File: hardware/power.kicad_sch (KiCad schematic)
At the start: 31 parts, among them J2 batt, Q1 AO3400A, SW57 MK-12C02-G020, U3 BQ24075RGT, U4 TLV62569DBV

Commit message: Add MY-18650-01 footprint and 3d model
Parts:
- removed J2: batt, Battery:BatteryHolder_Keystone_1042_1x18650, symbol Connector_Generic:Conn_01x02
- added J2, J5: MY-18650-01, lib:MY-18650-01, symbol Connector:Conn_01x01_Socket
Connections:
- net GND: now also J2.1 (Pin_1)
- net at C3.1, U3.2 (BAT), U3.3 (BAT): now also J5.1 (Pin_1)
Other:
- note added: "Battery terminals"
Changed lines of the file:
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@@
 		)
 	)
+	(rectangle
+		(start 156.21 132.08)
+		(end 165.1 139.7)
+		(stroke
+			(width 0)
+			(type dash)
+		)
+		(fill
+			(type none)
+		)
+	)
 	(image
 		(at 222.25 39.37)
@@
 		)
 	)
+	(text "Battery\nterminals"
+		(exclude_from_sim no)
+		(at 160.782 142.24 0)
+		(effects
+			(font
+				(size 1.27 1.27)
+			)
+		)
+	)
 	(text "100mA"
 		(exclude_from_sim no)
@@
 	)
 	(symbol
+		(lib_id "Connector:Conn_01x01_Socket")
+		(at 161.29 137.16 0)
+		(unit 1)
+		(exclude_from_sim no)
+		(in_bom yes)
+		(on_board yes)
+		(dnp no)
+		(property "Reference" "J2"
+			(at 162.306 137.16 0)
+			(effects
+				(font
+					(size 1.27 1.27)
+				)
+				(justify left)
+			)
+		)
+		(property "Value" "MY-18650-01"
+			(at 162.56 138.4299 0)
+			(effects
+				(font
+					(size 1.27 1.27)
+				)
+				(justify left)
+				(hide yes)
+			)
+		)
+		(property "Footprint" "lib:MY-18650-01"
+			(at 161.29 137.16 0)
+			(effects
+				(font
+					(size 1.27 1.27)
+				)
+				(hide yes)
+			)
+		)
+		(property "Datasheet" "~"
+			(at 161.29 137.16 0)
+			(effects
+				(font
+					(size 1.27 1.27)
+				)
+				(hide yes)
+			)
+		)
+		(property "Description" "Generic connector, single row, 01x01, script generated"
+			(at 161.29 137.16 0)
+			(effects
+				(font
+					(size 1.27 1.27)
+				)
+				(hide yes)
+			)
+		)
+		(property "LCSC" "C2979183"
+			(at 161.29 137.16 0)
+			(effects
+				(font
+					(size 1.27 1.27)
+				)
+				(hide yes)
+			)
+		)
+		(pin "1"
+		)
+		(instances
+			(project "badge"
+				(path "/dc4a3d77-b0f8-4e90-a4be-3e93c7025348/fa1edb42-107e-4301-94d6-2222638475c5"
+					(reference "J2")
+					(unit 1)
+				)
+			)
+		)
+	)
+	(symbol
 		(lib_id "power:VDD")
 		(at 113.03 31.75 0)
@@
 	)
 	(symbol
-		(lib_id "Connector_Generic:Conn_01x02")
-		(at 161.29 137.16 0)
-		(mirror x)
-		(unit 1)
-		(exclude_from_sim no)
-		(in_bom yes)
-		(on_board yes)
-		(dnp no)
-		(property "Reference" "J2"
-			(at 161.544 132.08 0)
-			(effects
-				(font
-					(size 1.27 1.27)
-				)
-			)
-		)
-		(property "Value" "batt"
-			(at 161.29 139.954 0)
-			(effects
-				(font
-					(size 1.27 1.27)
-				)
-			)
-		)
-		(property "Footprint" "Battery:BatteryHolder_Keystone_1042_1x18650"
-			(at 161.29 137.16 0)
-			(effects
-				(font
-					(size 1.27 1.27)
-				)
-				(hide yes)
-			)
-		)
-		(property "Datasheet" "~"
-			(at 161.29 137.16 0)
-			(effects
-				(font
-					(size 1.27 1.27)
-				)
-				(hide yes)
-			)
-		)
-		(property "Description" "Generic connector, single row, 01x02, script generated (kicad-library-utils/schlib/autogen/connector/)"
-			(at 161.29 137.16 0)
-			(effects
-				(font
-					(size 1.27 1.27)
-				)
-				(hide yes)
-			)
-		)
-		(pin "2"
-		)
-		(pin "1"
-		)
-		(instances
-			(project "badge"
-				(path "/dc4a3d77-b0f8-4e90-a4be-3e93c7025348/fa1edb42-107e-4301-94d6-2222638475c5"
-					(reference "J2")
-					(unit 1)
-				)
-			)
-		)
-	)
-	(symbol
 		(lib_id "power:GND")
 		(at 113.03 58.42 0)
@@
 					(unit 1)
 				)
+			)
+		)
+	)
+	(symbol
+		(lib_id "Connector:Conn_01x01_Socket")
+		(at 161.29 134.62 0)
+		(unit 1)
+		(exclude_from_sim no)
+		(in_bom yes)
+		(on_board yes)
+		(dnp no)
+		(property "Reference" "J5"
+			(at 162.306 134.62 0)
+			(effects
+				(font
+					(size 1.27 1.27)
+				)
+				(justify left)
+			)
+		)
+		(property "Value" "MY-18650-01"
+			(at 162.56 135.8899 0)
+			(effects
+				(font
+					(size 1.27 1.27)
+				)
+				(justify left)
+				(hide yes)
+			)
+		)
+		(property "Footprint" "lib:MY-18650-01"
+			(at 161.29 134.62 0)
+			(effects
+				(font
+					(size 1.27 1.27)
+				)
+				(hide yes)
+			)
+		)
+		(property "Datasheet" "~"
+			(at 161.29 134.62 0)
+			(effects
+				(font
+					(size 1.27 1.27)
+				)
+				(hide yes)
+			)
+		)
+		(property "Description" "Generic connector, single row, 01x01, script generated"
+			(at 161.29 134.62 0)
+			(effects
+				(font
+					(size 1.27 1.27)
+				)
+				(hide yes)
+			)
+		)
+		(property "LCSC" "C2979183"
+			(at 161.29 134.62 0)
+			(effects
+				(font
+					(size 1.27 1.27)
+				)
+				(hide yes)
+			)
+		)
+		(pin "1"
+		)
+		(instances
+			(project "badge"
+				(path "/dc4a3d77-b0f8-4e90-a4be-3e93c7025348/fa1edb42-107e-4301-94d6-2222638475c5"
+					(reference "J5")
+					(unit 1)
+				)

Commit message: Cleanup project library
Add hexpansion connector symbol, footprint and 3d
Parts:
- J2, J5: footprint lib:MY-18650-01 -> badge:MY-18650-01
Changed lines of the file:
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@@
 			)
 		)
-		(property "Footprint" "lib:MY-18650-01"
+		(property "Footprint" "badge:MY-18650-01"
 			(at 161.29 137.16 0)
 			(effects
@@
 			)
 		)
-		(property "Footprint" "lib:MY-18650-01"
+		(property "Footprint" "badge:MY-18650-01"
 			(at 161.29 134.62 0)
 			(effects

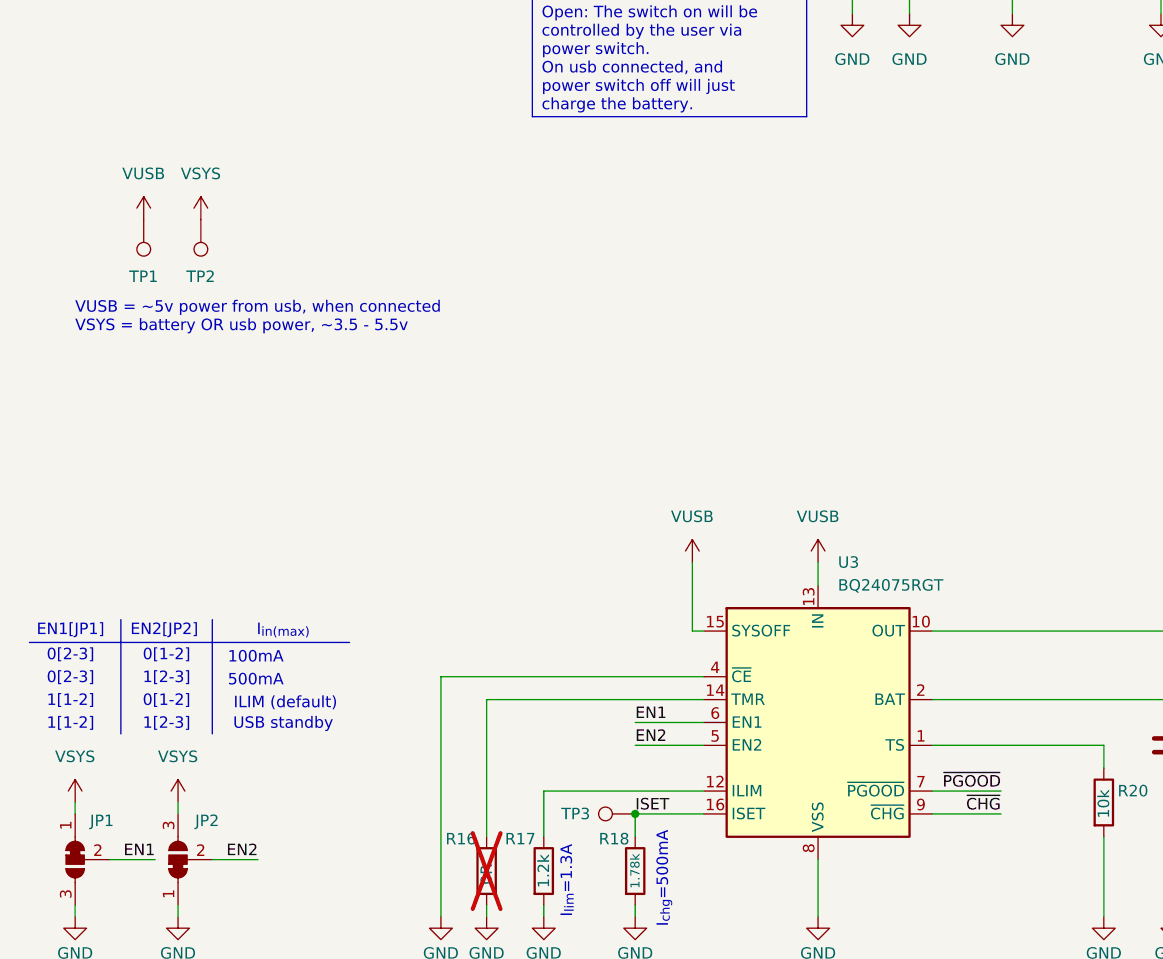
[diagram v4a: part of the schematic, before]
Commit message: Route all board
Fix CS missing for SD card
Add IMU symbol and footprint to the project lib
Finish esp32 pinswaps
Move non critical signals to the keyboard IO expander
Add power flag symbols
Fix Dpad pin type
Fix IMU pin type
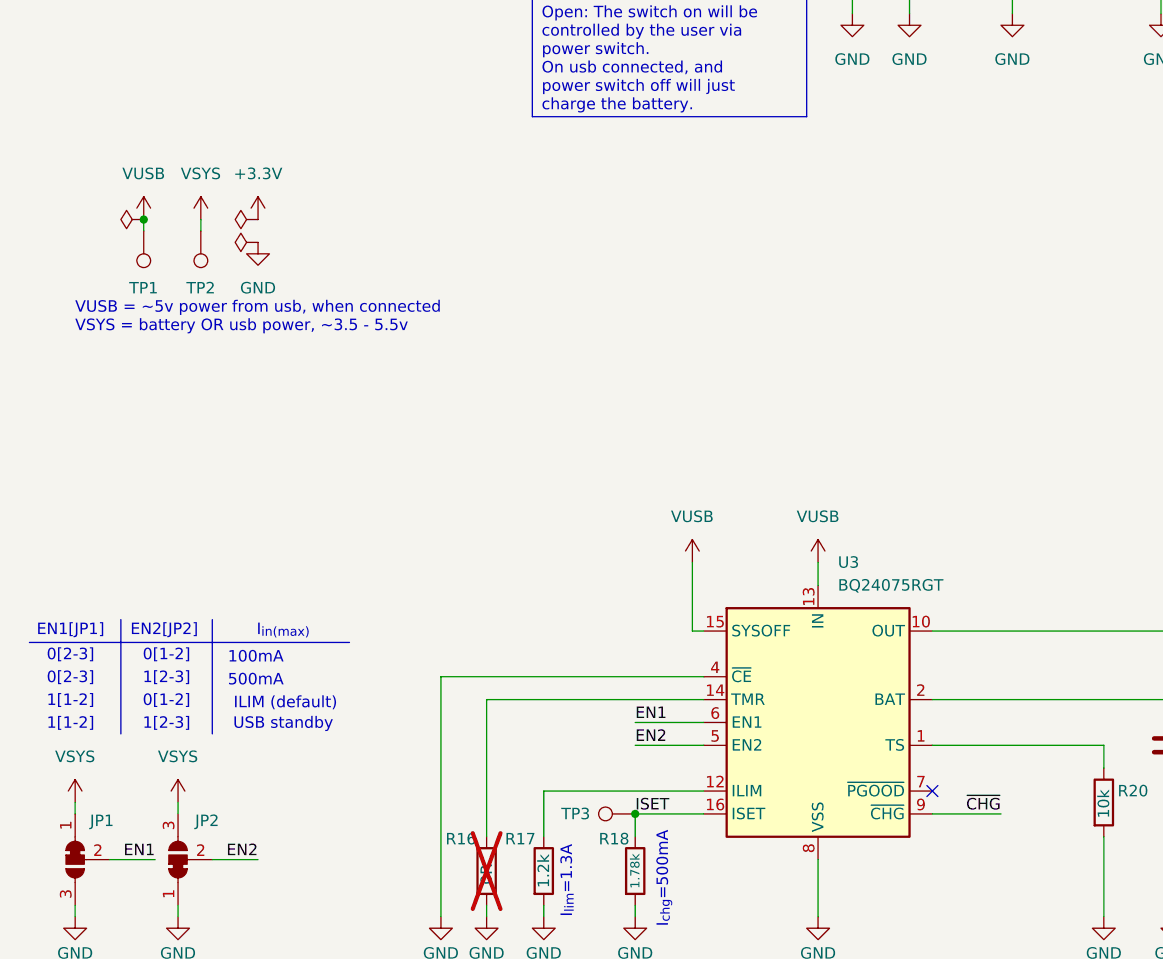
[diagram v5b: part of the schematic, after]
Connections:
- net ~{PGOOD}: no longer names the net of U3.7 (~{PGOOD})
- no-connect marks 0 -> 1
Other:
- moved on the sheet: TP1, TP2

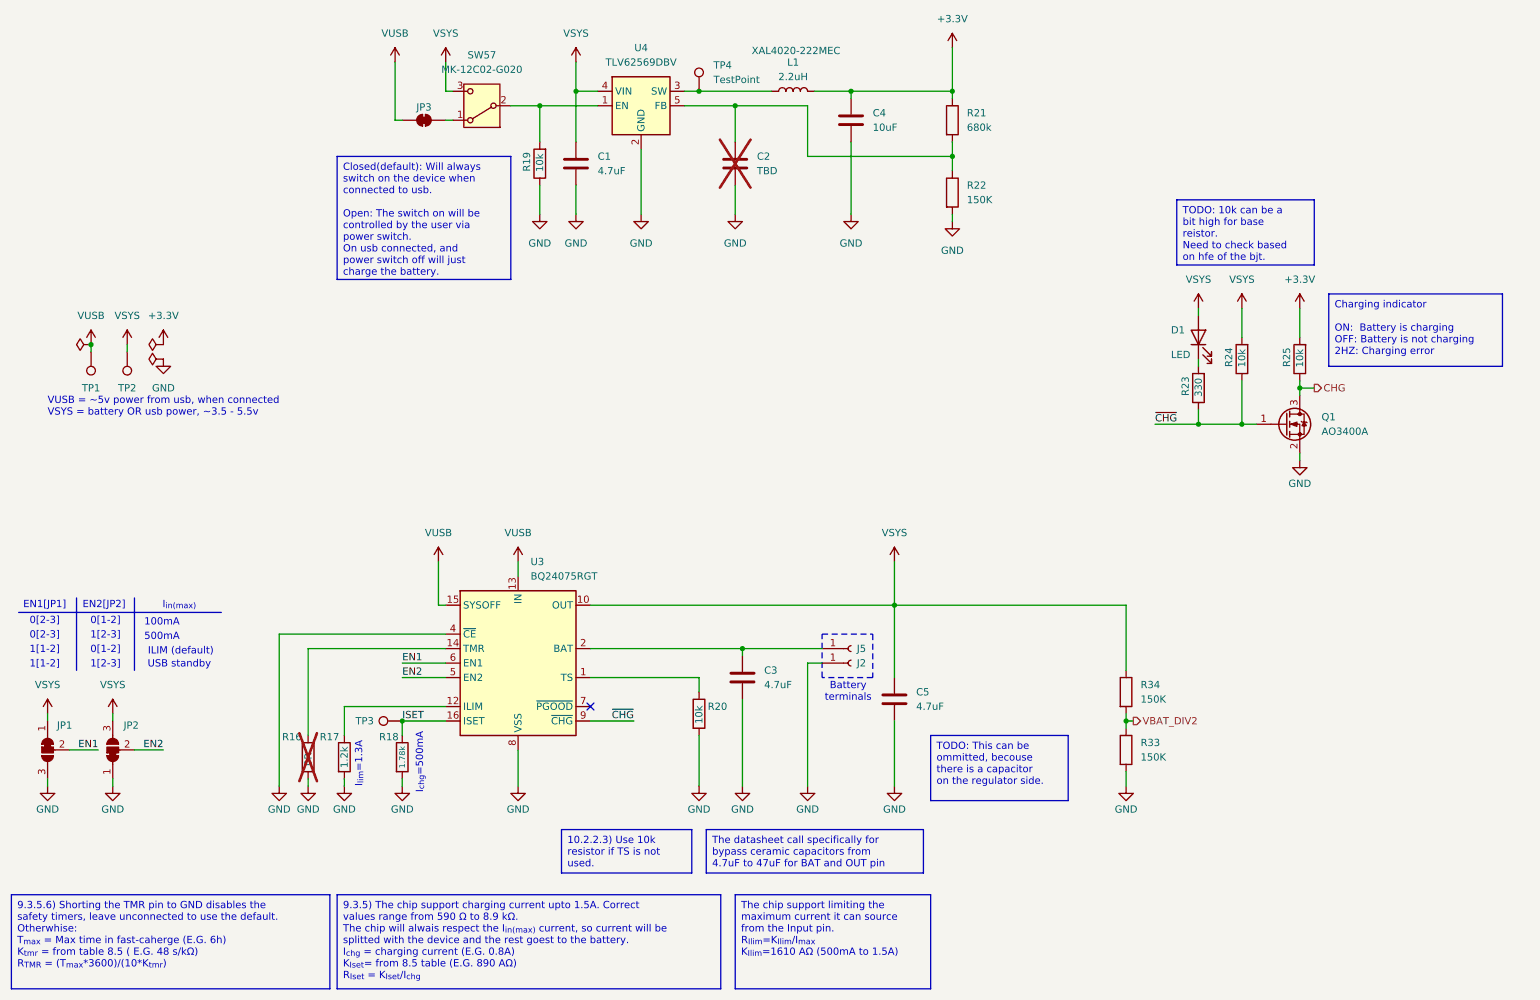
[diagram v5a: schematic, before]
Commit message: Associate all LCSC component
Change sdcard pullup resistor to 47K
Center main schematic
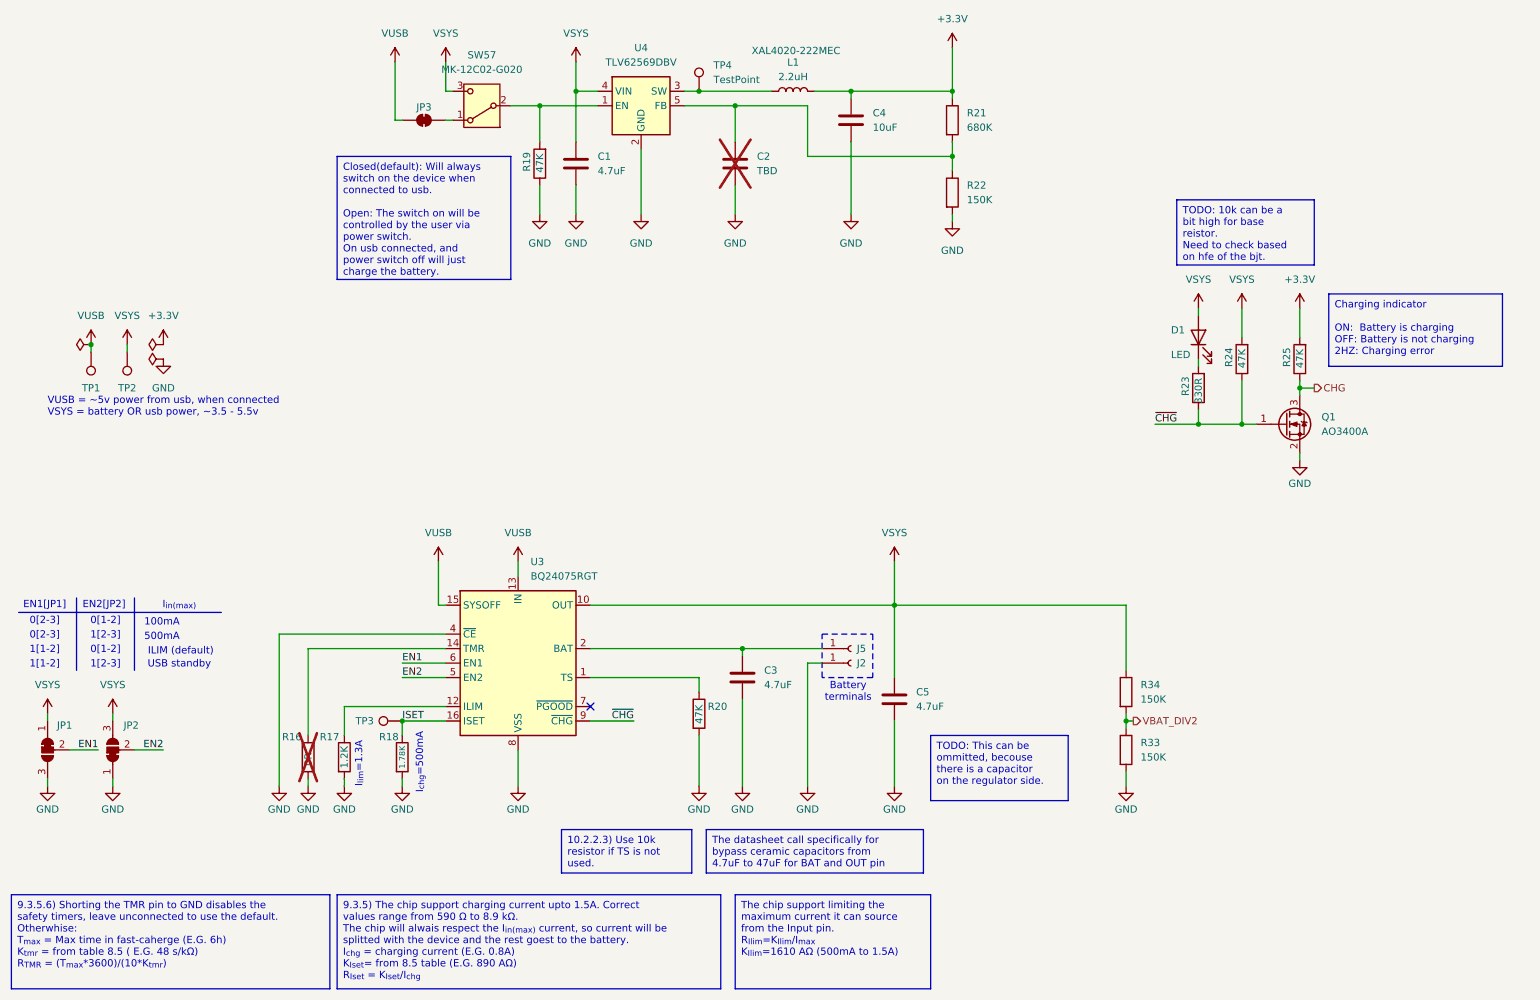
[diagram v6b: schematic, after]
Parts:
- C1, C3, C5: LCSC (none) -> C1705
- C4: LCSC (none) -> C1691
- D1: LCSC (none) -> C965799
- R16: LCSC (none) -> C116699
- R17: value 1.2k -> 1.2K; LCSC (none) -> C114605
- R18: value 1.78k -> 1.78K; LCSC (none) -> C137775
- R19, R20, R24, R25: value 10k -> 47K; LCSC (none) -> C105579
- R21: value 680k -> 680K; LCSC (none) -> C137690
- R22, R33, R34: LCSC (none) -> C114660
- R23: value 330 -> 330R; LCSC (none) -> C105879
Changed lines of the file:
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@@
 			)
 		)
+		(property "LCSC" "C965799"
+			(at 222.25 80.01 0)
+			(effects
+				(font
+					(size 1.27 1.27)
+				)
+				(hide yes)
+			)
+		)
 		(pin "2"
 		)
@@
 			)
 		)
-		(property "Value" "680k"
+		(property "Value" "680K"
 			(at 181.61 43.1799 0)
 			(effects
@@
 			)
 		)
+		(property "LCSC" "C137690"
+			(at 179.07 41.91 0)
+			(effects
+				(font
+					(size 1.27 1.27)
+				)
+				(hide yes)
+			)
+		)
 		(pin "2"
 		)
@@
 			)
 		)
+		(property "LCSC" "C1705"
+			(at 113.03 49.53 0)
+			(effects
+				(font
+					(size 1.27 1.27)
+				)
+				(hide yes)
+			)
+		)
 		(pin "2"
 		)
@@
 			)
 		)
+		(property "LCSC" "C114660"
+			(at 209.55 152.4 0)
+			(effects
+				(font
+					(size 1.27 1.27)
+				)
+				(hide yes)
+			)
+		)
 		(pin "2"
 		)
@@
 			)
 		)
-		(property "Value" "10k"
+		(property "Value" "47K"
 			(at 106.68 47.752 90)
 			(effects
@@
 			)
 		)
+		(property "LCSC" "C105579"
+			(at 106.68 49.53 0)
+			(effects
+				(font
+					(size 1.27 1.27)
+				)
+				(hide yes)
+			)
+		)
 		(pin "2"
 		)
@@
 			)
 		)
-		(property "Value" "1.78k"
+		(property "Value" "1.78K"
 			(at 82.55 153.67 90)
 			(effects
@@
 			)
 		)
+		(property "LCSC" "C137775"
+			(at 82.55 153.67 0)
+			(effects
+				(font
+					(size 1.27 1.27)
+				)
+				(hide yes)
+			)
+		)
 		(pin "2"
 		)
@@
 			)
 		)
-		(property "Value" "10k"
+		(property "Value" "47K"
 			(at 229.87 82.042 90)
 			(effects
@@
 			)
 		)
+		(property "LCSC" "C105579"
+			(at 229.87 83.82 0)
+			(effects
+				(font
+					(size 1.27 1.27)
+				)
+				(hide yes)
+			)
+		)
 		(pin "2"
 		)
@@
 			)
 		)
+		(property "LCSC" "C1705"
+			(at 142.24 139.7 0)
+			(effects
+				(font
+					(size 1.27 1.27)
+				)
+				(hide yes)
+			)
+		)
 		(pin "2"
 		)
@@
 			)
 		)
-		(property "Value" "1.2k"
+		(property "Value" "1.2K"
 			(at 72.39 153.67 90)
 			(effects
@@
 			)
 		)
+		(property "LCSC" "C114605"
+			(at 72.39 153.67 0)
+			(effects
+				(font
+					(size 1.27 1.27)
+				)
+				(hide yes)
+			)
+		)
 		(pin "2"
 		)
@@
 			)
 		)
+		(property "LCSC" "C114660"
+			(at 179.07 54.61 0)
+			(effects
+				(font
+					(size 1.27 1.27)
+				)
+				(hide yes)
+			)
+		)
 		(pin "2"
 		)
@@
 			)
 		)
-		(property "Value" "10k"
+		(property "Value" "47K"
 			(at 134.62 147.828 90)
 			(effects
@@
 			)
 		)
+		(property "LCSC" "C105579"
+			(at 134.62 146.05 0)
+			(effects
+				(font
+					(size 1.27 1.27)
+				)
+				(hide yes)
+			)
+		)
 		(pin "2"
 		)
@@
 			)
 		)
+		(property "LCSC" "C1691"
+			(at 161.29 41.91 0)
+			(effects
+				(font
+					(size 1.27 1.27)
+				)
+				(hide yes)
+			)
+		)
 		(pin "2"
 		)
@@
 			)
 		)
-		(property "Value" "10k"
+		(property "Value" "47K"
 			(at 240.03 82.042 90)
 			(effects
@@
 			)
 		)
+		(property "LCSC" "C105579"
+			(at 240.03 83.82 0)
+			(effects
+				(font
+					(size 1.27 1.27)
+				)
+				(hide yes)
+			)
+		)
 		(pin "2"
 		)
@@
 			)
 		)
+		(property "LCSC" "C116699"
+			(at 66.04 153.67 0)
+			(effects
+				(font
+					(size 1.27 1.27)
+				)
+				(hide yes)
+			)
+		)
 		(pin "2"
 		)
@@
 			)
 		)
+		(property "LCSC" "C114660"
+			(at 209.55 142.24 0)
+			(effects
+				(font
+					(size 1.27 1.27)
+				)
+				(hide yes)
+			)
+		)
 		(pin "2"
 		)
@@
 			)
 		)
-		(property "Value" "330"
+		(property "Value" "330R"
 			(at 222.25 87.122 90)
 			(effects
@@
 			)
 		)
+		(property "LCSC" "C105879"
+			(at 222.25 88.9 0)
+			(effects
+				(font
+					(size 1.27 1.27)
+				)
+				(hide yes)
+			)
+		)
 		(pin "2"
 		)
@@
 			(at 168.91 143.51 0)
 			(effects
+				(font
+					(size 1.27 1.27)
+				)
+				(hide yes)
+			)
+		)
+		(property "LCSC" "C1705"
+			(at 168.91 143.51 0)
+			(effects

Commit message: update bom, correct jlcpcb rotation
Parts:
- R18: LCSC C137775 -> C321755
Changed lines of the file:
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@@
 			)
 		)
-		(property "LCSC" "C137775"
+		(property "LCSC" "C321755"
 			(at 82.55 153.67 0)
 			(effects
